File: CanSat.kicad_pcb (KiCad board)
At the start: 2 copper layers, 55.6 x 55.5 mm, 72 parts, among them IC1 W25Q128JVPIQ, J1 USB_C_Receptacle, M1 SG-90, SW1 SW_Push, SW2 SW_Push, U1 MPU-6050, U2 RA-02_LORA, U5 RP2350_60QFN, U6 LM1085-5.0, U7 LM1085-3.3, U8 BMP280, U9 APS6404L-3SQR-ZR, Y2 ASE-12.000MHz-E-T

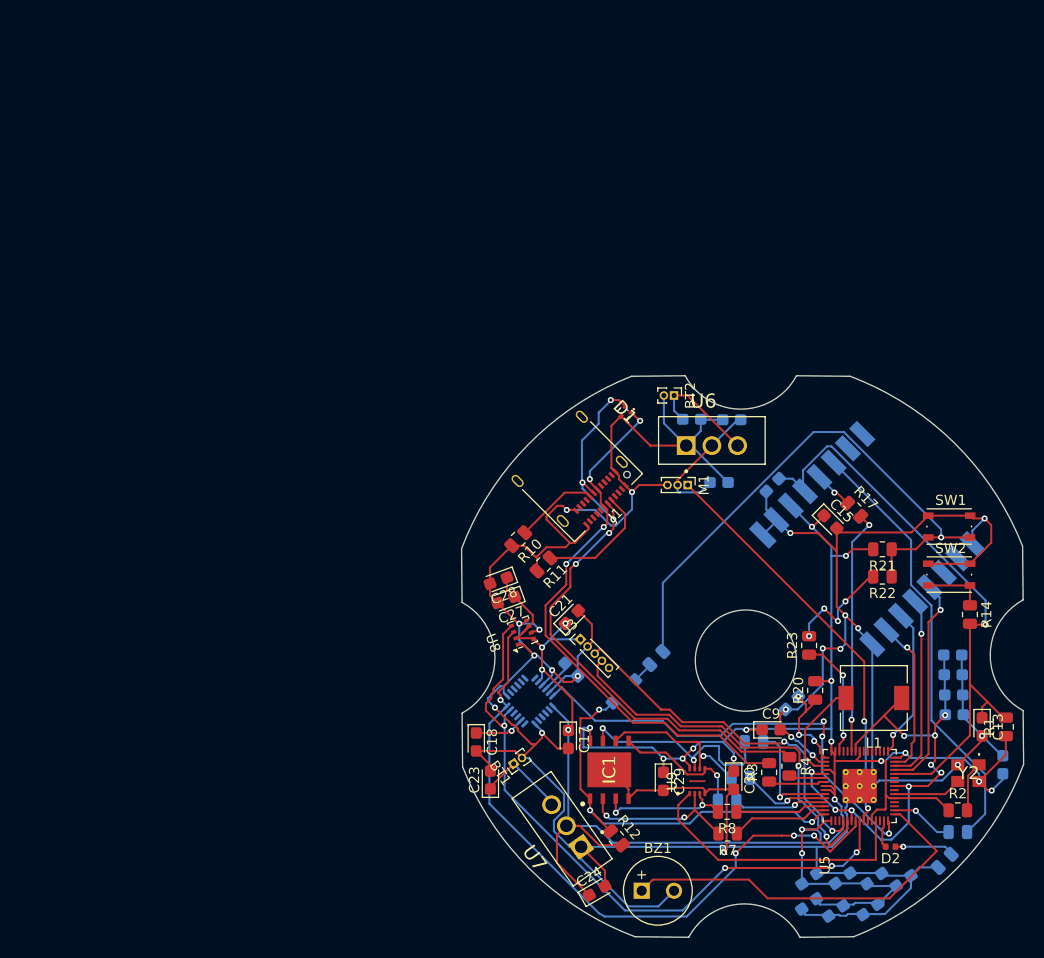
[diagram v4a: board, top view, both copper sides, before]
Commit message: Rotated LoRa and updated readme
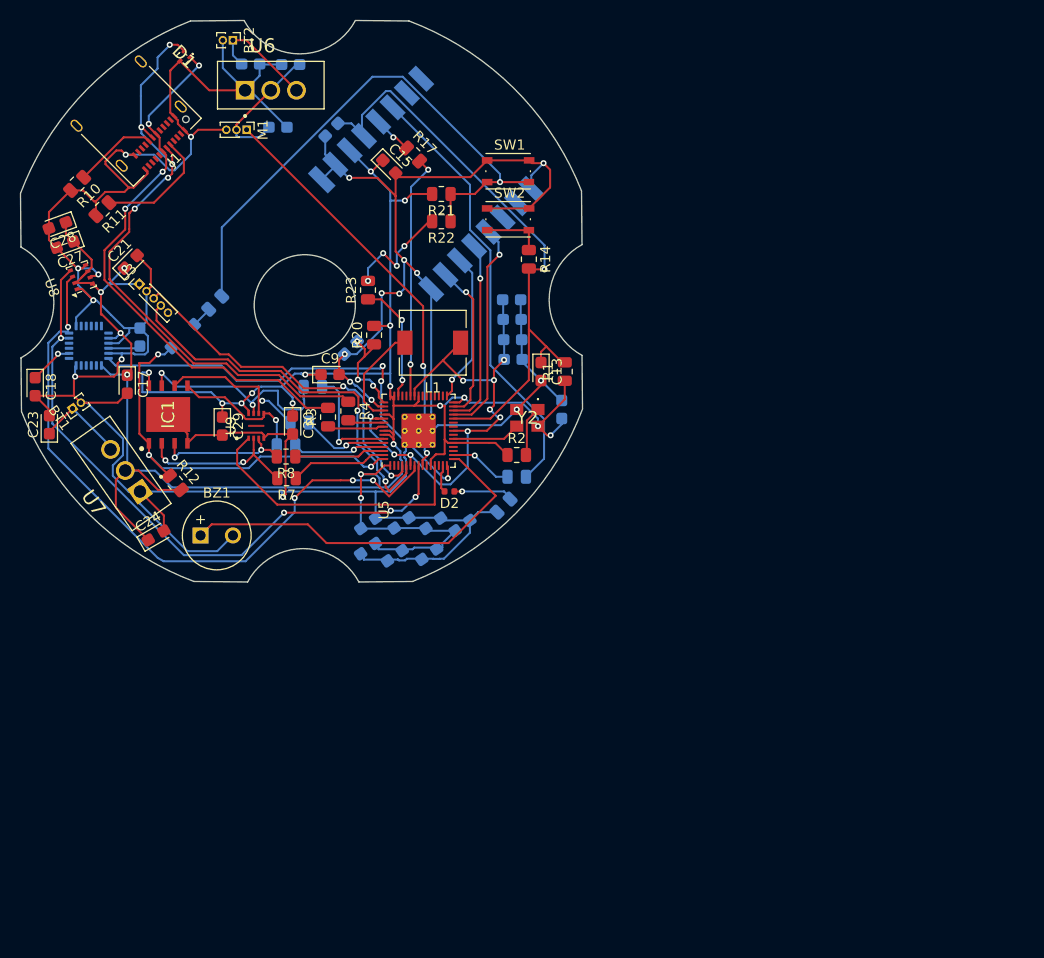
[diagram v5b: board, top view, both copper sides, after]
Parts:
- moved C14 56.0 mm to (129.9, 76.3)
- moved BT1 56.0 mm to (81.6, 76.2)
- moved BT2 56.0 mm to (97.5, 39.8)
- moved C1 56.0 mm to (110.8, 90.0)
- moved C10 56.0 mm to (125.0, 67.4)
- moved C2 56.0 mm to (113.5, 90.7)
- moved C22 56.0 mm to (107.2, 48.6)
- moved C23 56.0 mm to (79.3, 77.8)
- moved C25 56.0 mm to (99.2, 42.1)
- moved C27 56.0 mm to (80.8, 60.0)
- moved C28 56.0 mm to (80.1, 58.1)
- moved C5 56.0 mm to (114.1, 87.5)
- moved C7 56.0 mm to (120.1, 87.8)
- moved C9 56.0 mm to (107.0, 72.8)
- moved D1 56.0 mm to (92.5, 41.5)
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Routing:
- net /I2C0_SCL: track 65.4 -> 63.6 mm
- net /INT: track 45.5 -> 44.4 mm
- net Net-(U1-CPOUT): track 5.02 -> 4.42 mm
- net GND: track 359.6 -> 360.2 mm, vias 21 -> 19
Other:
- outline, holes or cut-outs redrawn

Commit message: Update of pcb
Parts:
- added M2: MountingHole_2.2mm_M2, MountingHole:MountingHole_2.2mm_M2, F.Cu at (106.7, 86.7)
- added M2: MountingHole_2.2mm_M2, MountingHole:MountingHole_2.2mm_M2, F.Cu at (129.2, 57.6)
- added REF**: MountingHole_2.2mm_M2, MountingHole:MountingHole_2.2mm_M2, F.Cu at (111.3, 41.1)
- added REF**: MountingHole_2.2mm_M2, MountingHole:MountingHole_2.2mm_M2, F.Cu at (79.5, 55.4)
- moved R10 2.62 mm to (83.6, 56.1)
- moved SW2 1.63 mm to (123.0, 57.5)
- moved R11 1.52 mm to (84.7, 58.0)
- moved C27 1.04 mm to (81.5, 60.8)
- moved C28 1.04 mm to (80.8, 58.9)
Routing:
- net GND: track 360.2 -> 333.9 mm
- net /~{PSRAM_CS}: track 28.1 -> 30.5 mm
- net /I2C0_SCL: track 63.6 -> 65.8 mm
- net Net-(J1-CC2): track 8.11 -> 9.67 mm
- net +3V3: track 241.5 -> 240.5 mm
- net Net-(J1-CC1): track 12.1 -> 13.1 mm
- net Net-(R14-Pad1): track 6.09 -> 6.77 mm
- added copper zone on B.Cu, net GND
- added copper zone on F.Cu, net GND

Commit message: Update CanSat.kicad_pcb
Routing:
- net GND: track 333.9 -> 336.3 mm
- net /~{PSRAM_CS}: track 30.5 -> 31.9 mm

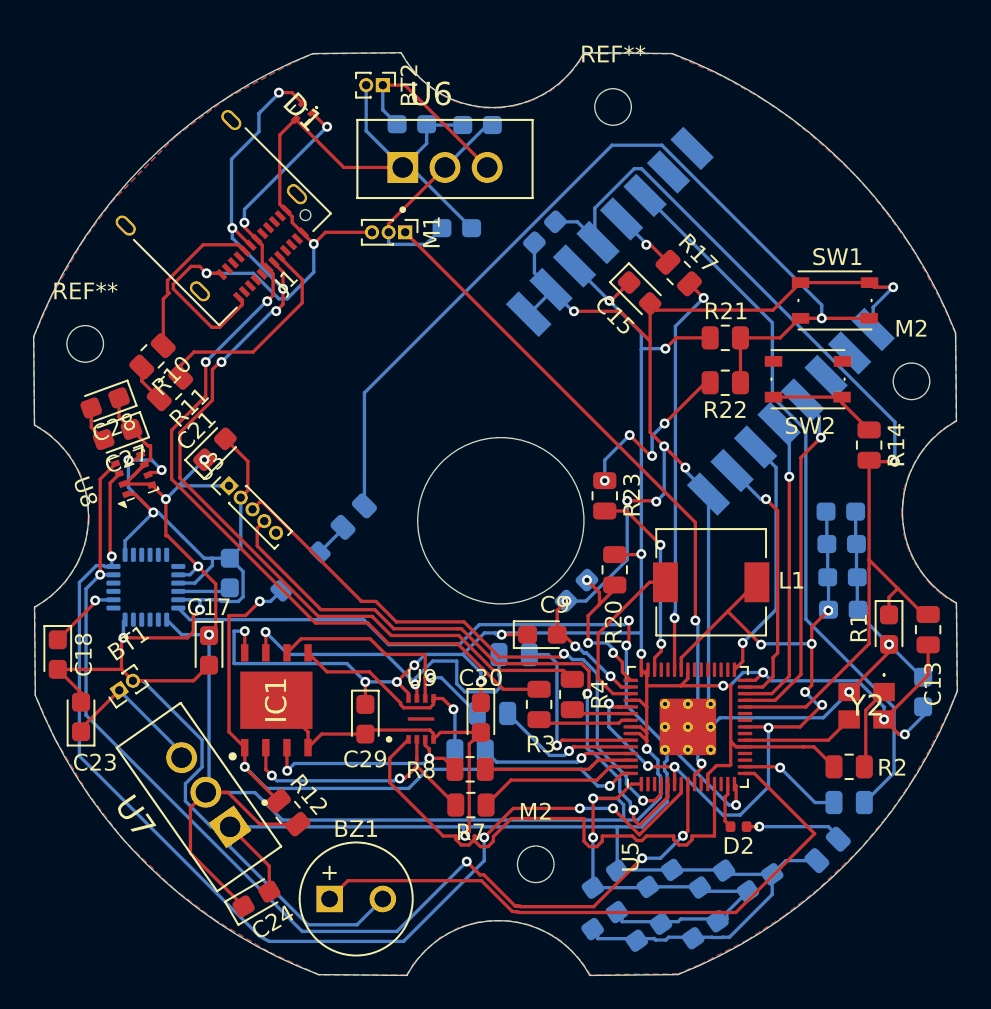
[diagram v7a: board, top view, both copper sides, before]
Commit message: Changed LoRa module to RFM98W 433MHz
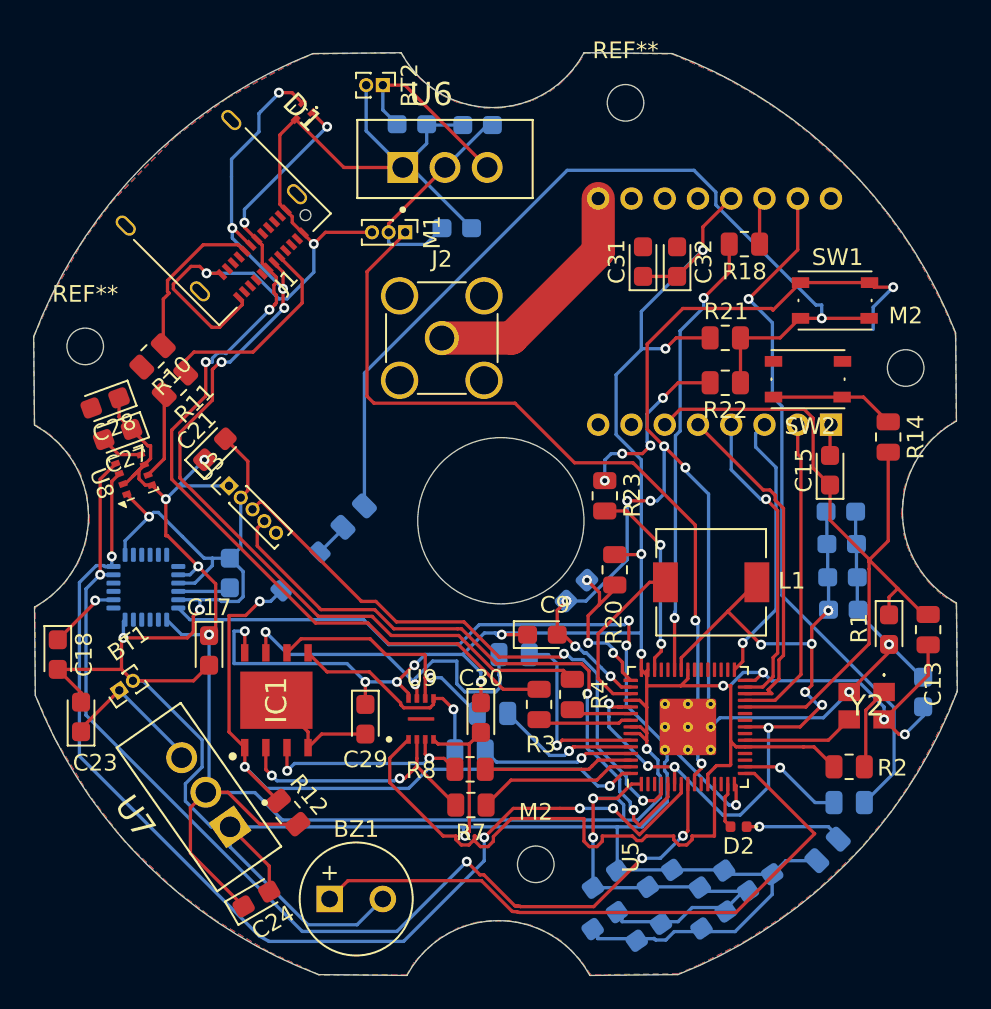
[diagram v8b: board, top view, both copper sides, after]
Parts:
- removed C22: 100nF, Capacitor_Tantalum_SMD:CP_EIA-2012-15_AVX-P
- removed R17: 100R, Resistor_SMD:R_0805_2012Metric
- removed U2: RA-02_LORA, RA-02_LORA:MODULE_RA-02_LORA
- added C31: 22u, Capacitor_Tantalum_SMD:CP_EIA-2012-15_AVX-P, F.Cu at (113.1, 50.4)
- added C32: 100n, Capacitor_Tantalum_SMD:CP_EIA-2012-15_AVX-P, F.Cu at (115.2, 50.4)
- added J2: Conn_Coaxial, Connector_Coaxial:SMA_Amphenol_901-144_Vertical, F.Cu at (101.0, 55.0)
- added R18: 100, Resistor_SMD:R_0805_2012Metric, F.Cu at (119.2, 49.4)
- added U4: RFM98W-433S2, RF_Module:HOPERF_RFM9XW_THT, B.Cu at (124.4, 60.2)
- C15: value 100nF -> 100n
- R15: value 10K -> 220
- moved C15 15.6 mm to (124.3, 63.0), turned to 90 degrees
- moved R14 1.25 mm to (127.8, 61.0)
- moved M2 0.87 mm to (128.9, 56.8)
- moved REF** 0.79 mm to (112.0, 40.9)
- moved C3 0.77 mm to (117.3, 90.0)
- moved R11 0.39 mm to (85.0, 57.8)
- moved REF** 0.15 mm to (79.5, 55.5)
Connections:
- C15 pad 1: +3V3 -> /~{RST}
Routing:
- net GND: track 336.3 -> 314.7 mm, vias 19 -> 16
- net Net-(J2-In): track 0.00 -> 14.7 mm
- net /~{RST}: track 61.3 -> 47.3 mm, vias 1 -> 0
- net /SERVO: track 40.8 -> 49.9 mm
- net +3V3: track 240.5 -> 249.0 mm
- net Net-(U2-DI00): track 3.91 -> 0.00 mm, vias 1 -> 0
- net Net-(U4-DIO0): track 0.00 -> 2.86 mm
- net /SPI0_SCK: track 15.8 -> 18.6 mm
- net /RADIO_RX_INT: track 24.3 -> 27.0 mm
- net /SPI0_RX: track 21.5 -> 19.1 mm, vias 1 -> 0
- net /SPI0_CSn: track 18.5 -> 20.6 mm, vias 1 -> 0
- net /SPI0_TX: track 14.9 -> 16.5 mm
- net /RADIO_RX_TIMEOUT: track 43.5 -> 41.9 mm, vias 0 -> 1
- net /USB_D-: track 55.1 -> 56.1 mm
- net Net-(R14-Pad1): track 6.77 -> 7.52 mm
